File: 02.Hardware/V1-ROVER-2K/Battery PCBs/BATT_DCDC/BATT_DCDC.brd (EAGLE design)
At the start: 32.8 x 16.8 mm, 54 parts, among them K3 FLEX8, Q1 NVTFS9D6P04M8LTAG, Q2 2N7002PW, Q5 2N7002PW, U1 MCP6071T-E/OT, U3 TPS55330RTET

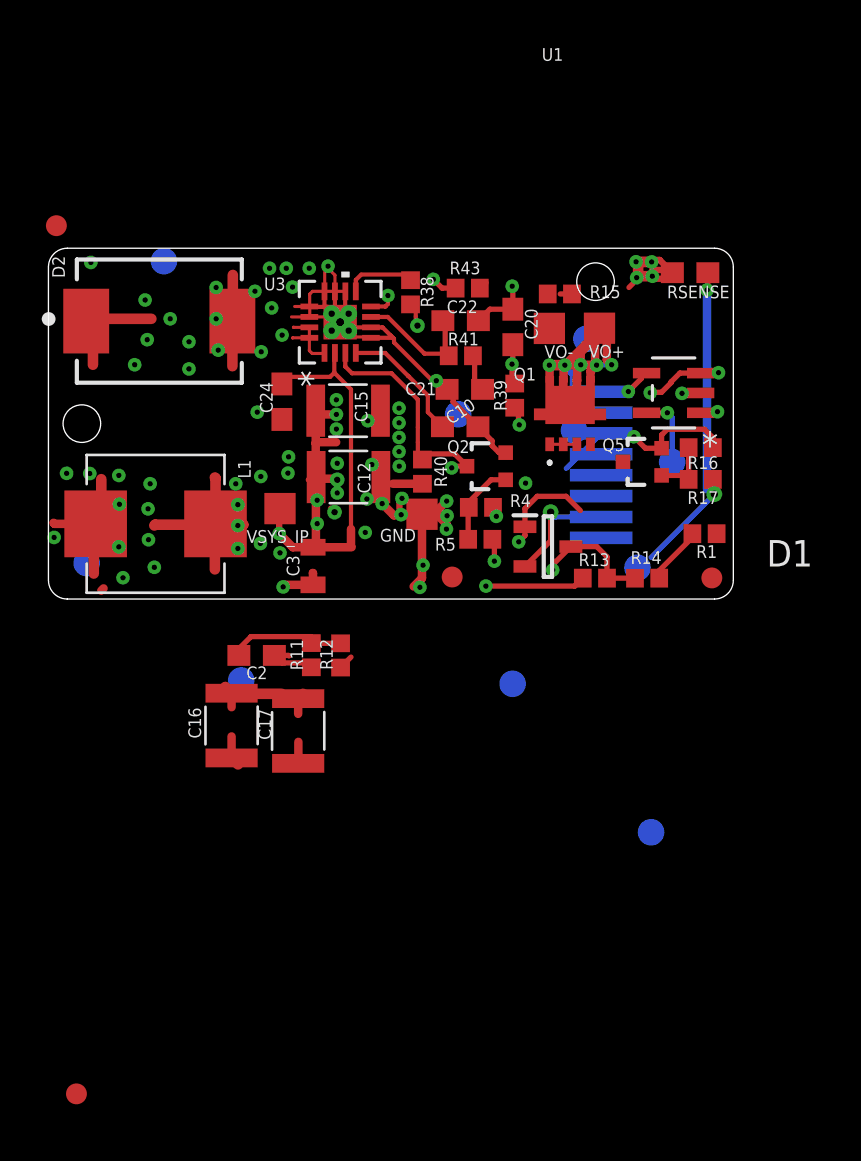
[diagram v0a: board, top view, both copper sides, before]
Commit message: Update DCDC
Colocacion y Posicionamiento de los componentes en la tarjeta.
Pendiente de Routeado.
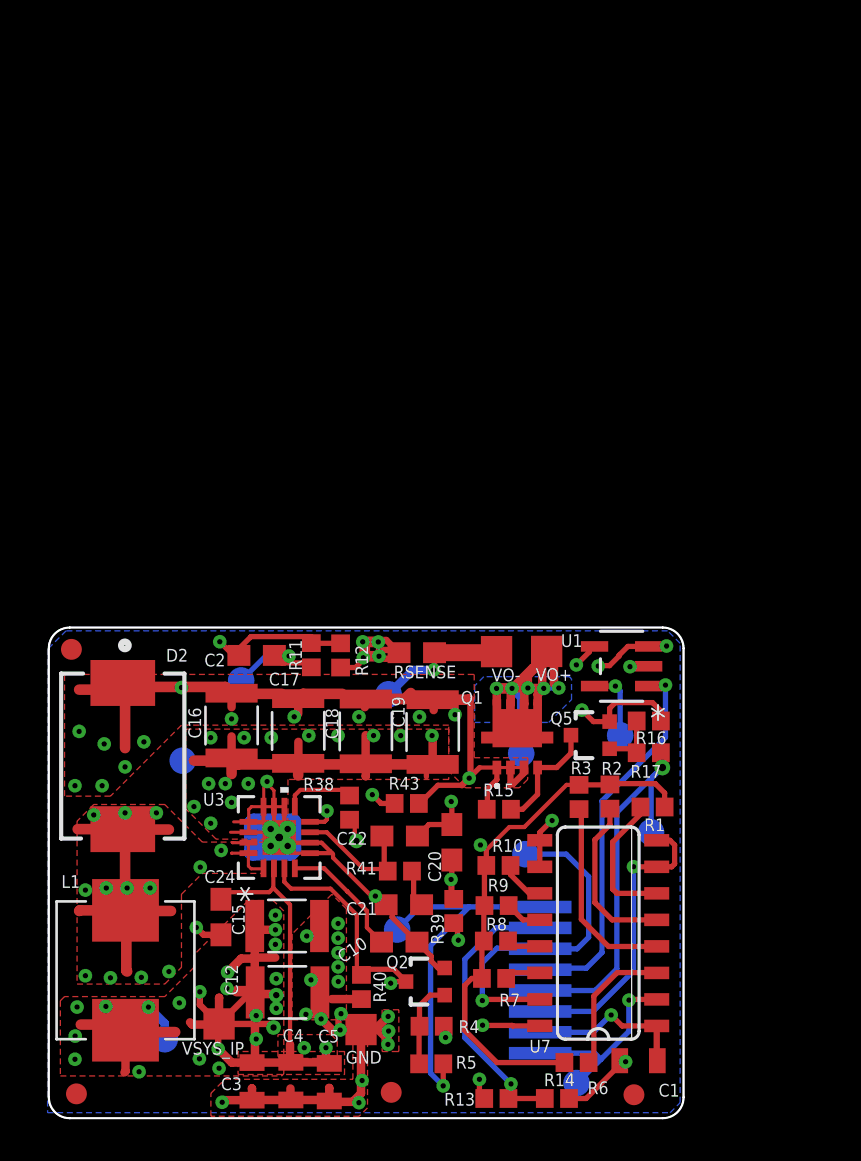
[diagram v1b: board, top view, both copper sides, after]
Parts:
- removed D1: BAT54S, BAT54S:SOT95P240X110-3N
- added C1, C4, C5: 10uF, SparkFun-Capacitors:0805
- added C18, C19: 47uF 25V, Wurth_Elektronik_Passive_Capacitors_rev19a:WCAP-CSGP_1210
- added R10: 82k, SparkFun-Resistors:0402
- added R2: 20k, SparkFun-Resistors:0402
- added R3: 10k, SparkFun-Resistors:0402
- added R6: 5k1, SparkFun-Resistors:0402
- added R7: 680k, SparkFun-Resistors:0402
- added R8: 330k, SparkFun-Resistors:0402
- added R9: 160k, SparkFun-Resistors:0402
- added U7: TPIC2810D, EDCPSU - Rev2:SO16
- C20: value N.A. -> 47nF
- R11: value 5k1 -> 15k
- R12: value 8k2 -> 1k
- R13: value 169k -> 15k
- R14: value 39k -> 15k
- R15: value 120k -> 470k
- R40: value N.A. -> 78.7k
- R43: value 47k -> 78.7k
- RSENSE: value 100mR -> 10mR
- moved U$1 50.0 mm to (49.6, 4.33)
- moved U$2 30.9 mm to (22.6, 25.7)
- moved R13 25.4 mm to (43.0, 4.15)
- moved R14 25.3 mm to (45.9, 4.15)
- moved R5 25.2 mm to (39.9, 5.81)
- moved R4 25.0 mm to (39.9, 7.61)
- moved #EN_DCDC_TP 24.9 mm to (38.2, 12.2)
- moved C10 24.9 mm to (38.3, 11.6)
- moved C21 24.9 mm to (38.5, 13.4)
- moved Q2 24.9 mm to (39.6, 9.75)
- moved R38 24.9 mm to (35.9, 18.1)
- moved R39 24.9 mm to (40.9, 13.1)
- moved R40 24.9 mm to (36.5, 9.49)
- moved R41 24.9 mm to (38.4, 15.0)
- moved R43 24.9 mm to (38.7, 18.3)
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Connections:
- new net N$10: R9.1, U7.12
- new net N$11: R10.1, U7.11
- new net N$2: R1.1, U7.6
- new net N$3: R2.1, U7.5
- new net N$5: R3.1, U7.4
- new net N$6: R6.1, U7.3
- new net N$7: R7.1, U7.14
- new net N$9: R8.1, U7.13
- net FB_TPS: now also R10.2, R2.2, R3.2, R6.2, R7.2, R8.2, R9.2
- net GND: now also C1.1, C18.1, C19.1, C4.1, C5.1, U7.10, U7.16, U7.7, U7.8, U7.9; no longer D1.1, R1.1
- net SCL: now also U7.15
- net SDA: now also U7.2
- net VCC: now also C1.2, U7.1; no longer D1.2
- net VOUTSENSE: no longer D1.3
- net VSOURCE: now also C18.2, C19.2
- net VSYS: now also C4.2, C5.2
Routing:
- net GND: track 80.8 -> 138.9 mm, vias 38 -> 49
- net ISENSE_RAW: track 3.67 -> 44.8 mm, vias 1 -> 2
- net FB_TPS: track 8.69 -> 37.1 mm, vias 2 -> 3
- net VSYS: track 38.6 -> 64.5 mm, vias 24 -> 25
- net VSOURCE: track 12.0 -> 37.8 mm, vias 7 -> 13
- net VCC: track 9.08 -> 27.2 mm
- net #EN_DCDC: track 1.08 -> 18.0 mm
- net SCL: track 2.48 -> 16.6 mm
- net OP_SWITCH: track 5.02 -> 18.7 mm
- net N$1: track 13.6 -> 26.7 mm, vias 1 -> 2
- net N$5: track 0.00 -> 9.48 mm
- net SDA: track 0.00 -> 9.42 mm, vias 0 -> 1
- net N$3: track 0.00 -> 8.10 mm
- net VOUTSENSE: track 5.77 -> 13.6 mm
- net N$6: track 0.00 -> 6.77 mm
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- added copper zone on layer 1, net GND
- added copper zone on layer 15, net GND
- added copper zone on layer 16, net GND
- added copper zone on layer 2, net GND
- added copper zone on layer 1, net SW2_TPS
- added copper zone on layer 2, net SW2_TPS
- added copper zone on layer 16, net VOUT+
- added copper zone on layer 1, net VSOURCE
- added copper zone on layer 2, net VSOURCE
- added copper zone on layer 1, net VSYS
- added copper zone on layer 2, net VSYS
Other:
- board size 32.8 x 16.8 mm -> 30.4 x 23.5 mm
- board text added: "BATT_DCDC v5-Jun'21"
